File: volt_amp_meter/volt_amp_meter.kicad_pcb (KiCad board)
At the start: 2 copper layers, 50 x 40 mm, 30 parts, among them J1 Molex, J2 ICSP, U2 PIC16F883-IP, U3 LM358, U4 L78L05_SOT89, Y1 4MHz

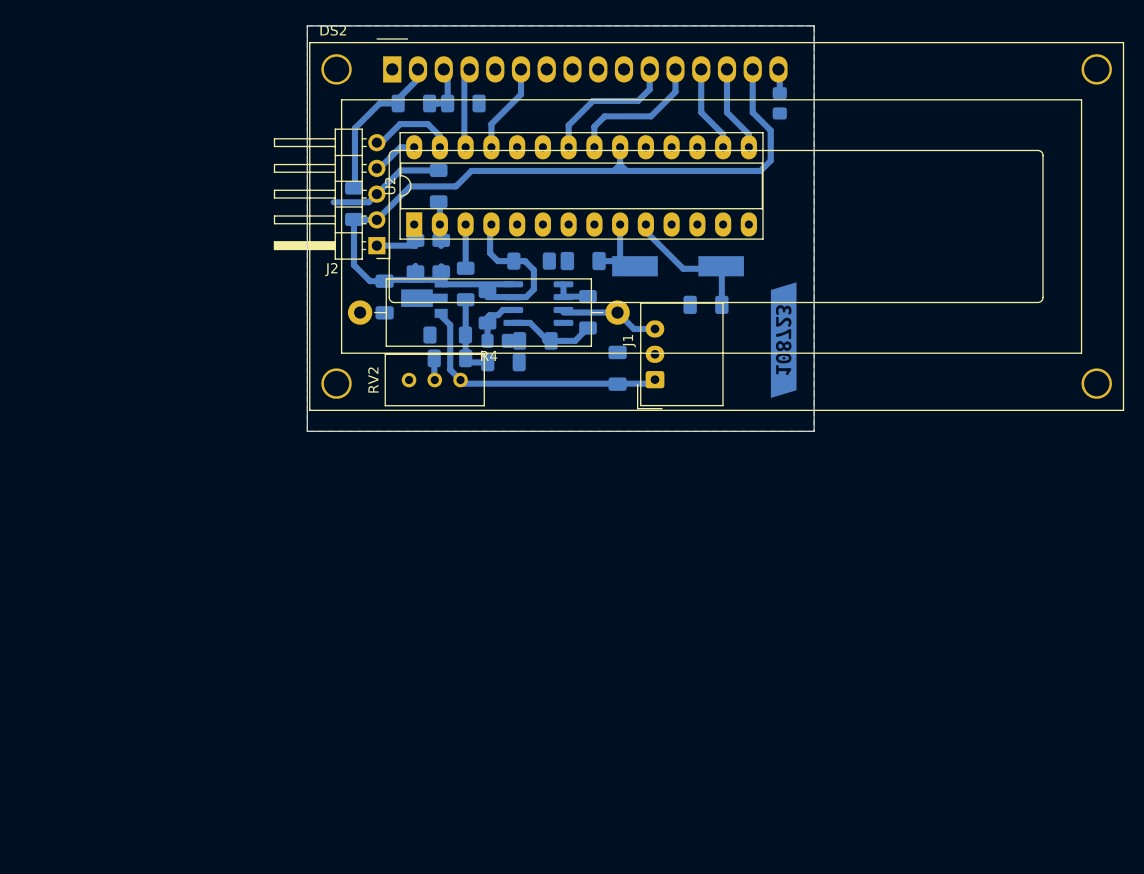
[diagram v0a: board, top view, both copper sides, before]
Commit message: [ADD] Panel volt-amp meter from 0-30V and 0-3A (minimal protections)
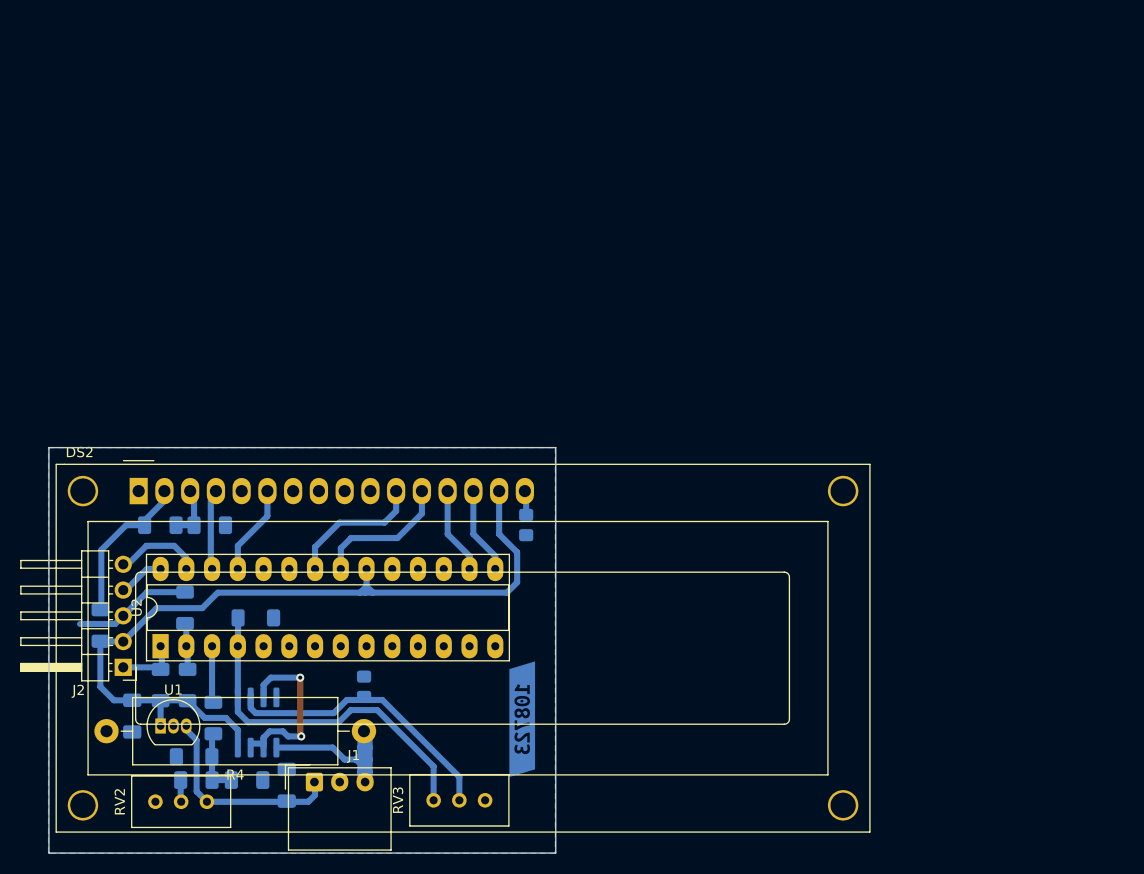
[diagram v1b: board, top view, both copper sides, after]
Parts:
- removed C4, C5: 22p, Capacitor_SMD:C_1206_3216Metric_Pad1.33x1.80mm_HandSolder
- removed R10, R9: 10k, Resistor_SMD:R_1206_3216Metric_Pad1.30x1.75mm_HandSolder
- removed R8: 1k, Resistor_SMD:R_1206_3216Metric_Pad1.30x1.75mm_HandSolder
- removed U4: L78L05_SOT89, Package_TO_SOT_SMD:SOT-89-3
- removed Y1: 4MHz, Crystal:Crystal_SMD_HC49-SD
- added RV3: 5k, Potentiometer_THT:Potentiometer_Bourns_3386C_Horizontal, F.Cu at (147.5, 110.4)
- added U1: L78L05_TO92, Package_TO_SOT_THT:TO-92_Inline, F.Cu at (120.5, 103.1)
- moved C1 52.5 mm to (133.0, 108.9)
- moved J1 52.0 mm to (135.7, 108.6), turned to 0 degrees
- moved U3 49.8 mm to (130.0, 102.7), turned to -90 degrees
- moved R11 49.5 mm to (125.7, 102.3)
- moved R12 49.2 mm to (120.5, 99.0)
- moved R6 49.2 mm to (123.2, 99.0)
- moved R14 48.5 mm to (125.4, 83.3)
- moved R15 48.5 mm to (120.5, 83.3)
- moved D1 48.5 mm to (123.8, 106.1)
- moved DS2 48.5 mm to (118.4, 79.9)
- moved J2 48.5 mm to (116.8, 97.3)
- moved R1 48.5 mm to (156.6, 83.2)
- moved R16 48.5 mm to (114.6, 93.2)
- moved R2 48.5 mm to (124.1, 108.4)
- moved R5 48.5 mm to (122.9, 91.4)
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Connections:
- R7 pad 1: Net-(U3B--) -> Net-(U3A--)
- U2 pad 10: Net-(U2-CLKOUT/OSC2/RA6) -> unconnected-(U2-CLKOUT/OSC2/RA6-Pad10)
- U2 pad 9: Net-(U2-CLKIN/OSC1/RA7) -> unconnected-(U2-CLKIN/OSC1/RA7-Pad9)
- U3 pad 1: Net-(U3A--) -> /I_{meas}
- U3 pad 3: /I_{sense} -> Net-(U3A-+)
- U3 pad 5: Net-(U3B-+) -> /I_{sense}
- U3 pad 6: Net-(U3B--) -> Net-(U3A-+)
- U3 pad 7: /I_{meas} -> Net-(U3A-+)
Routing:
- net Net-(U3A--): track 3.71 -> 27.9 mm
- net /I_{meas}: track 15.6 -> 34.8 mm
- net Net-(U3A-+): track 0.00 -> 17.4 mm, vias 0 -> 2
- net Net-(U2-CLKOUT/OSC2/RA6): track 12.1 -> 0.00 mm
- net Net-(U2-CLKIN/OSC1/RA7): track 9.37 -> 0.00 mm
- net Net-(U3B-+): track 8.78 -> 0.00 mm
- net /I_{sense}: track 9.70 -> 18.3 mm
- net VCC: track 26.6 -> 20.5 mm
- net Net-(U3B--): track 5.16 -> 0.00 mm
- net +5V: track 84.3 -> 79.9 mm
- net Net-(D1-K): track 8.13 -> 6.55 mm
- net /VCC_{meas}: track 4.75 -> 5.77 mm
- net unconnected-(U2-CLKOUT/OSC2/RA6-Pad10): track 0.00 -> 0.69 mm
